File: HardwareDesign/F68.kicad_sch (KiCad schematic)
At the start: 2 parts, among them J001 Conn_02x40_Odd_Even

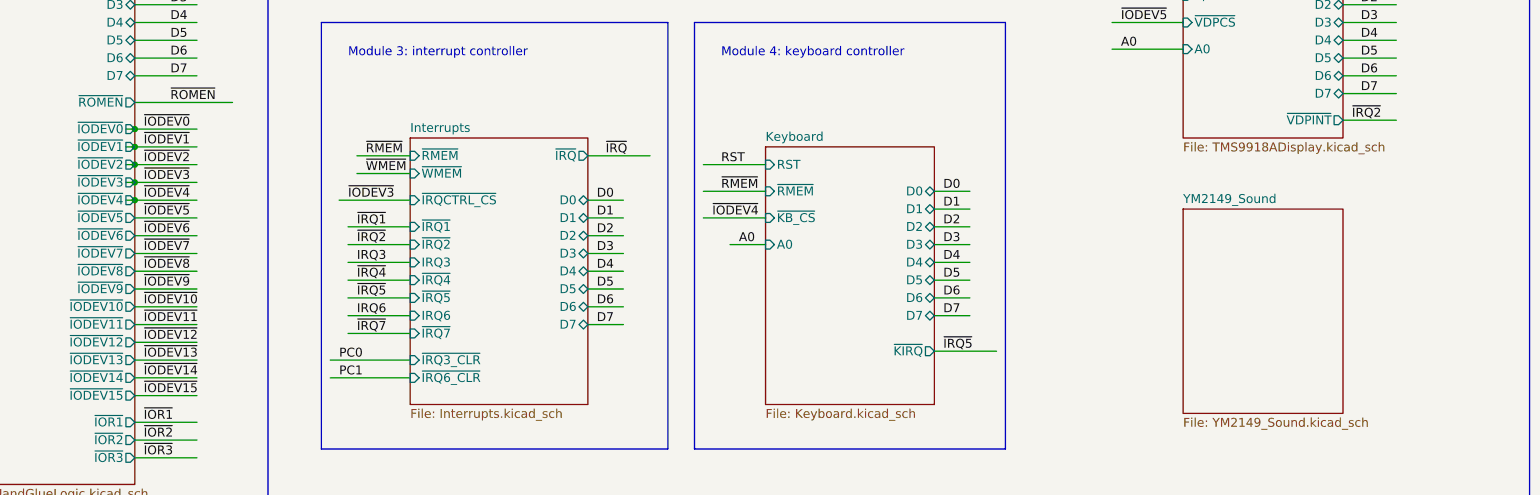
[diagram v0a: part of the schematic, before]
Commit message: connect backplane signals to YM2149 module
Also, tested the output circuit using 3.3 uF caps,
and it worked fine. 4.7 uF caps will probably also be
fine.
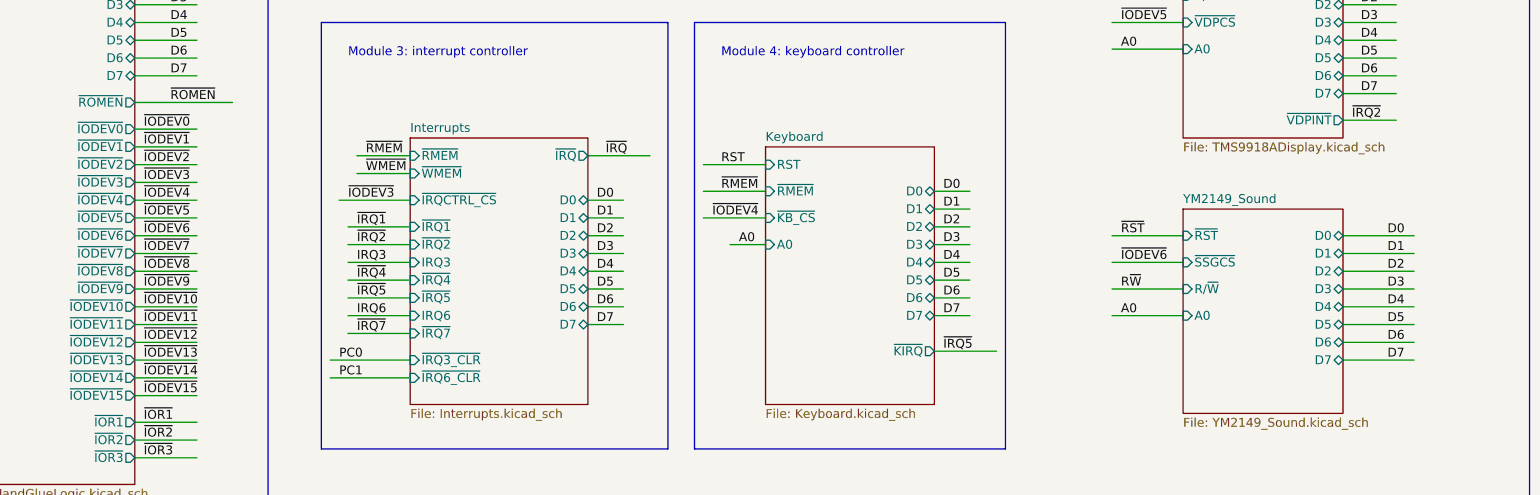
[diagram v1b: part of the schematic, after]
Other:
- sheet YM2149_Sound ports: added A0, D0, D1, D2, D3, D4, D5, D6, D7, R/~{W}, ~{RST}, ~{SSGCS}; removed none
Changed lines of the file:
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@@
 (kicad_sch (version 20211123) (generator eeschema)
   (paper "User" 359.994 278.206)
-  (junction (at 66.04 125.73) (diameter 0) (color 0 0 0 0)
-  )
-  (junction (at 66.04 118.11) (diameter 0) (color 0 0 0 0)
-  )
-  (junction (at 66.04 123.19) (diameter 0) (color 0 0 0 0)
-  )
-  (junction (at 66.04 120.65) (diameter 0) (color 0 0 0 0)
-  )
-  (junction (at 66.04 128.27) (diameter 0) (color 0 0 0 0)
-  )
   (wire (pts (xy 102.87 82.55) (xy 107.95 82.55))
     (stroke (width 0) (type default) (color 0 0 0 0))
@@
     (stroke (width 0) (type default) (color 0 0 0 0))
   )
-  (wire (pts (xy 64.77 123.19) (xy 66.04 123.19))
-    (stroke (width 0) (type default) (color 0 0 0 0))
-  )
-  (wire (pts (xy 64.77 120.65) (xy 66.04 120.65))
+  (wire (pts (xy 238.76 135.89) (xy 248.92 135.89))
     (stroke (width 0) (type default) (color 0 0 0 0))
   )
@@
     (stroke (width 0) (type default) (color 0 0 0 0))
   )
+  (wire (pts (xy 238.76 138.43) (xy 248.92 138.43))
+    (stroke (width 0) (type default) (color 0 0 0 0))
+  )
+  (wire (pts (xy 205.74 140.97) (xy 215.9 140.97))
+    (stroke (width 0) (type default) (color 0 0 0 0))
+  )
   (wire (pts (xy 179.07 72.39) (xy 189.23 72.39))
     (stroke (width 0) (type default) (color 0 0 0 0))
@@
     (stroke (width 0) (type default) (color 0 0 0 0))
   )
+  (wire (pts (xy 238.76 133.35) (xy 248.92 133.35))
+    (stroke (width 0) (type default) (color 0 0 0 0))
+  )
   (wire (pts (xy 274.32 118.11) (xy 288.29 118.11))
     (stroke (width 0) (type default) (color 0 0 0 0))
@@
     (stroke (width 0) (type default) (color 0 0 0 0))
   )
-  (wire (pts (xy 64.77 118.11) (xy 66.04 118.11))
-    (stroke (width 0) (type default) (color 0 0 0 0))
-  )
   (wire (pts (xy 153.67 36.83) (xy 146.05 36.83))
     (stroke (width 0) (type default) (color 0 0 0 0))
@@
     (stroke (width 0) (type default) (color 0 0 0 0))
   )
-  (wire (pts (xy 64.77 125.73) (xy 66.04 125.73))
+  (wire (pts (xy 238.76 146.05) (xy 248.92 146.05))
     (stroke (width 0) (type default) (color 0 0 0 0))
   )
@@
     (stroke (width 0) (type default) (color 0 0 0 0))
   )
-  (wire (pts (xy 64.77 128.27) (xy 66.04 128.27))
-    (stroke (width 0) (type default) (color 0 0 0 0))
-  )
   (wire (pts (xy 300.99 118.11) (xy 314.96 118.11))
     (stroke (width 0) (type default) (color 0 0 0 0))
@@
     (stroke (width 0) (type default) (color 0 0 0 0))
   )
+  (wire (pts (xy 205.74 144.78) (xy 215.9 144.78))
+    (stroke (width 0) (type default) (color 0 0 0 0))
+  )
   (wire (pts (xy 107.95 88.9) (xy 97.79 88.9))
     (stroke (width 0) (type default) (color 0 0 0 0))
@@
     (stroke (width 0) (type default) (color 0 0 0 0))
   )
+  (wire (pts (xy 205.74 133.35) (xy 215.9 133.35))
+    (stroke (width 0) (type default) (color 0 0 0 0))
+  )
   (wire (pts (xy 146.05 45.72) (xy 153.67 45.72))
     (stroke (width 0) (type default) (color 0 0 0 0))
@@
     (stroke (width 0) (type default) (color 0 0 0 0))
   )
+  (wire (pts (xy 238.76 148.59) (xy 248.92 148.59))
+    (stroke (width 0) (type default) (color 0 0 0 0))
+  )
   (wire (pts (xy 274.32 148.59) (xy 288.29 148.59))
     (stroke (width 0) (type default) (color 0 0 0 0))
@@
     (stroke (width 0) (type default) (color 0 0 0 0))
   )
+  (wire (pts (xy 238.76 143.51) (xy 248.92 143.51))
+    (stroke (width 0) (type default) (color 0 0 0 0))
+  )
   (wire (pts (xy 274.32 64.77) (xy 288.29 64.77))
     (stroke (width 0) (type default) (color 0 0 0 0))
@@
     (stroke (width 0) (type default) (color 0 0 0 0))
   )
+  (wire (pts (xy 205.74 137.16) (xy 215.9 137.16))
+    (stroke (width 0) (type default) (color 0 0 0 0))
+  )
   (wire (pts (xy 66.04 160.02) (xy 74.93 160.02))
     (stroke (width 0) (type default) (color 0 0 0 0))
@@
     (stroke (width 0) (type default) (color 0 0 0 0))
   )
+  (wire (pts (xy 238.76 151.13) (xy 248.92 151.13))
+    (stroke (width 0) (type default) (color 0 0 0 0))
+  )
   (wire (pts (xy 66.04 110.49) (xy 74.93 110.49))
     (stroke (width 0) (type default) (color 0 0 0 0))
@@
   )
   (wire (pts (xy 153.67 39.37) (xy 146.05 39.37))
+    (stroke (width 0) (type default) (color 0 0 0 0))
+  )
+  (wire (pts (xy 238.76 140.97) (xy 248.92 140.97))
     (stroke (width 0) (type default) (color 0 0 0 0))
   )
@@
     (effects (font (size 1.27 1.27)) (justify left bottom))
   )
+  (label "D5" (at 245.11 146.05 0)
+    (effects (font (size 1.27 1.27)) (justify left bottom))
+  )
   (label "D6" (at 180.34 49.53 0)
     (effects (font (size 1.27 1.27)) (justify left bottom))
@@
     (effects (font (size 1.27 1.27)) (justify left bottom))
   )
+  (label "A0" (at 207.01 144.78 0)
+    (effects (font (size 1.27 1.27)) (justify left bottom))
+  )
   (label "~{IODEV1}" (at 144.78 52.07 0)
     (effects (font (size 1.27 1.27)) (justify left bottom))
@@
     (effects (font (size 1.27 1.27)) (justify left bottom))
   )
+  (label "R~{W}" (at 207.01 140.97 0)
+    (effects (font (size 1.27 1.27)) (justify left bottom))
+  )
   (label "A3" (at 71.12 58.42 0)
     (effects (font (size 1.27 1.27)) (justify left bottom))
@@
     (effects (font (size 1.27 1.27)) (justify left bottom))
   )
+  (label "D0" (at 245.11 133.35 0)
+    (effects (font (size 1.27 1.27)) (justify left bottom))
+  )
   (label "~{RMEM}" (at 307.34 138.43 0)
     (effects (font (size 1.27 1.27)) (justify left bottom))
@@
     (effects (font (size 1.27 1.27)) (justify left bottom))
   )
+  (label "D6" (at 245.11 148.59 0)
+    (effects (font (size 1.27 1.27)) (justify left bottom))
+  )
   (label "RST" (at 147.32 34.29 0)
     (effects (font (size 1.27 1.27)) (justify left bottom))
@@
     (effects (font (size 1.27 1.27)) (justify left bottom))
   )
+  (label "D1" (at 245.11 135.89 0)
+    (effects (font (size 1.27 1.27)) (justify left bottom))
+  )
   (label "D1" (at 241.3 97.79 0)
     (effects (font (size 1.27 1.27)) (justify left bottom))
@@
     (effects (font (size 1.27 1.27)) (justify left bottom))
   )
+  (label "~{IODEV6}" (at 207.01 137.16 0)
+    (effects (font (size 1.27 1.27)) (justify left bottom))
+  )
   (label "~{IODEV1}" (at 67.31 120.65 0)
     (effects (font (size 1.27 1.27)) (justify left bottom))
@@
     (effects (font (size 1.27 1.27)) (justify left bottom))
   )
+  (label "D4" (at 245.11 143.51 0)
+    (effects (font (size 1.27 1.27)) (justify left bottom))
+  )
   (label "D5" (at 71.12 105.41 0)
     (effects (font (size 1.27 1.27)) (justify left bottom))
@@
     (effects (font (size 1.27 1.27)) (justify left bottom))
   )
+  (label "~{RST}" (at 207.01 133.35 0)
+    (effects (font (size 1.27 1.27)) (justify left bottom))
+  )
   (label "~{IODEV9}" (at 276.86 130.81 0)
     (effects (font (size 1.27 1.27)) (justify left bottom))
@@
     (effects (font (size 1.27 1.27)) (justify left bottom))
   )
+  (label "D2" (at 245.11 138.43 0)
+    (effects (font (size 1.27 1.27)) (justify left bottom))
+  )
   (label "~{IRQ5}" (at 181.61 149.86 0)
     (effects (font (size 1.27 1.27)) (justify left bottom))
@@
     (effects (font (size 1.27 1.27)) (justify left bottom))
   )
+  (label "D3" (at 245.11 140.97 0)
+    (effects (font (size 1.27 1.27)) (justify left bottom))
+  )
   (label "A4" (at 71.12 60.96 0)
     (effects (font (size 1.27 1.27)) (justify left bottom))
@@
   )
   (label "PC4" (at 180.34 69.85 0)
+    (effects (font (size 1.27 1.27)) (justify left bottom))
+  )
+  (label "D7" (at 245.11 151.13 0)
     (effects (font (size 1.27 1.27)) (justify left bottom))
   )
@@
       (effects (font (size 1.27 1.27)) (justify left top))
     )
-  )
+    (pin "D4" bidirectional (at 238.76 143.51 0)
+      (effects (font (size 1.27 1.27)) (justify right))
+    )
+    (pin "D5" bidirectional (at 238.76 146.05 0)
+      (effects (font (size 1.27 1.27)) (justify right))
+    )
+    (pin "D7" bidirectional (at 238.76 151.13 0)
+      (effects (font (size 1.27 1.27)) (justify right))
+    )
+    (pin "D6" bidirectional (at 238.76 148.59 0)
+      (effects (font (size 1.27 1.27)) (justify right))
+    )
+    (pin "D0" bidirectional (at 238.76 133.35 0)
+      (effects (font (size 1.27 1.27)) (justify right))
+    )
+    (pin "D2" bidirectional (at 238.76 138.43 0)
+      (effects (font (size 1.27 1.27)) (justify right))
+    )
+    (pin "D3" bidirectional (at 238.76 140.97 0)
+      (effects (font (size 1.27 1.27)) (justify right))
+    )
+    (pin "D1" bidirectional (at 238.76 135.89 0)
+      (effects (font (size 1.27 1.27)) (justify right))
+    )
+    (pin "~{SSGCS}" input (at 215.9 137.16 180)
+      (effects (font (size 1.27 1.27)) (justify left))
+    )
+    (pin "R{slash}~{W}" input (at 215.9 140.97 180)
+      (effects (font (size 1.27 1.27)) (justify left))
+    )
+    (pin "A0" input (at 215.9 144.78 180)
+      (effects (font (size 1.27 1.27)) (justify left))
+    )
+    (pin "~{RST}" input (at 215.9 133.35 180)
+      (effects (font (size 1.27 1.27)) (justify left))
+    )
+  )

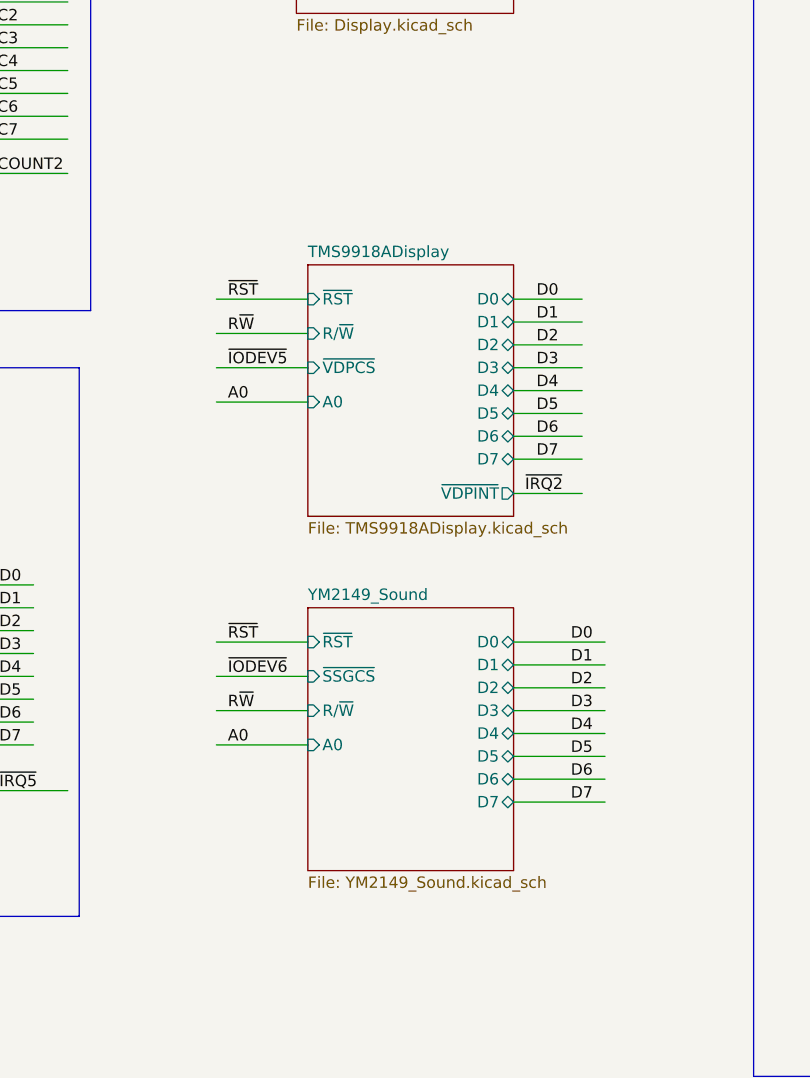
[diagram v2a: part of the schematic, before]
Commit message: lots of changes to TMS9918A and YM2149 modules
Changed the TMS9918A circuit to use -RMEM and -WMEM rather than R/-W,
since -RMEM and -WMEM are properly synchronized with E and the overall
CPU bus cycle. (Duh!)

Also chnaged the YM2149 circuit to use -RMEM and -WMEM. However,
it's less clear that this is a desirable change, because we would
like BDIR and BC1 to change "at the same time", and only when
the chip is being accessed. However, if the chip select is asserted
before -RMEM/-WMEM are asserted, then meaningless BDIR and BC1
values are going to be generated, which is not good. Need to think
about this.
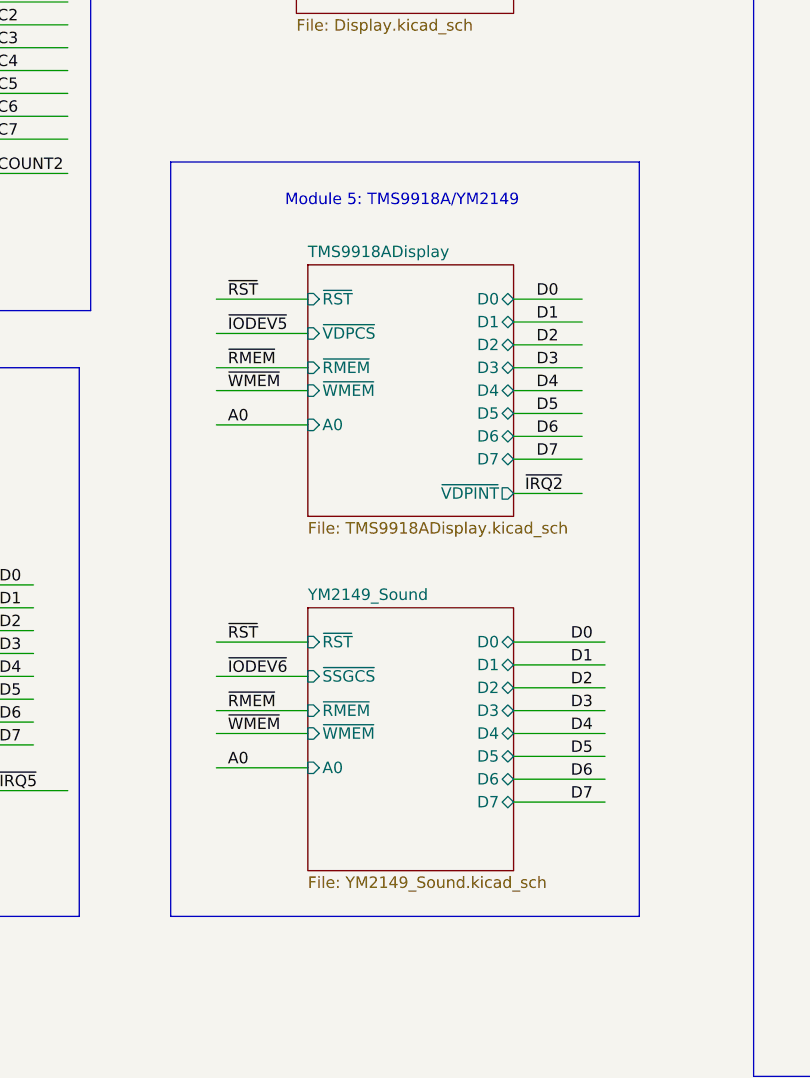
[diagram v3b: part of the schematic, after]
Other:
- sheet TMS9918ADisplay ports: added ~{RMEM}, ~{WMEM}; removed R/~{W}
- sheet YM2149_Sound ports: added ~{RMEM}, ~{WMEM}; removed R/~{W}
- note added: "Module 5: TMS9918A/YM2149"
